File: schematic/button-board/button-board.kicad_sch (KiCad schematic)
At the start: 30 parts, among them J10 Screw_Terminal_01x04, J11 Screw_Terminal_01x04, J3 Screw_Terminal_01x02, J4 Screw_Terminal_01x04, J5 Screw_Terminal_01x04, J6 Screw_Terminal_01x04, J7 Screw_Terminal_01x04, J8 Screw_Terminal_01x04, J9 Screw_Terminal_01x04, U1 MCP23017_SO, U2 ULN2803A

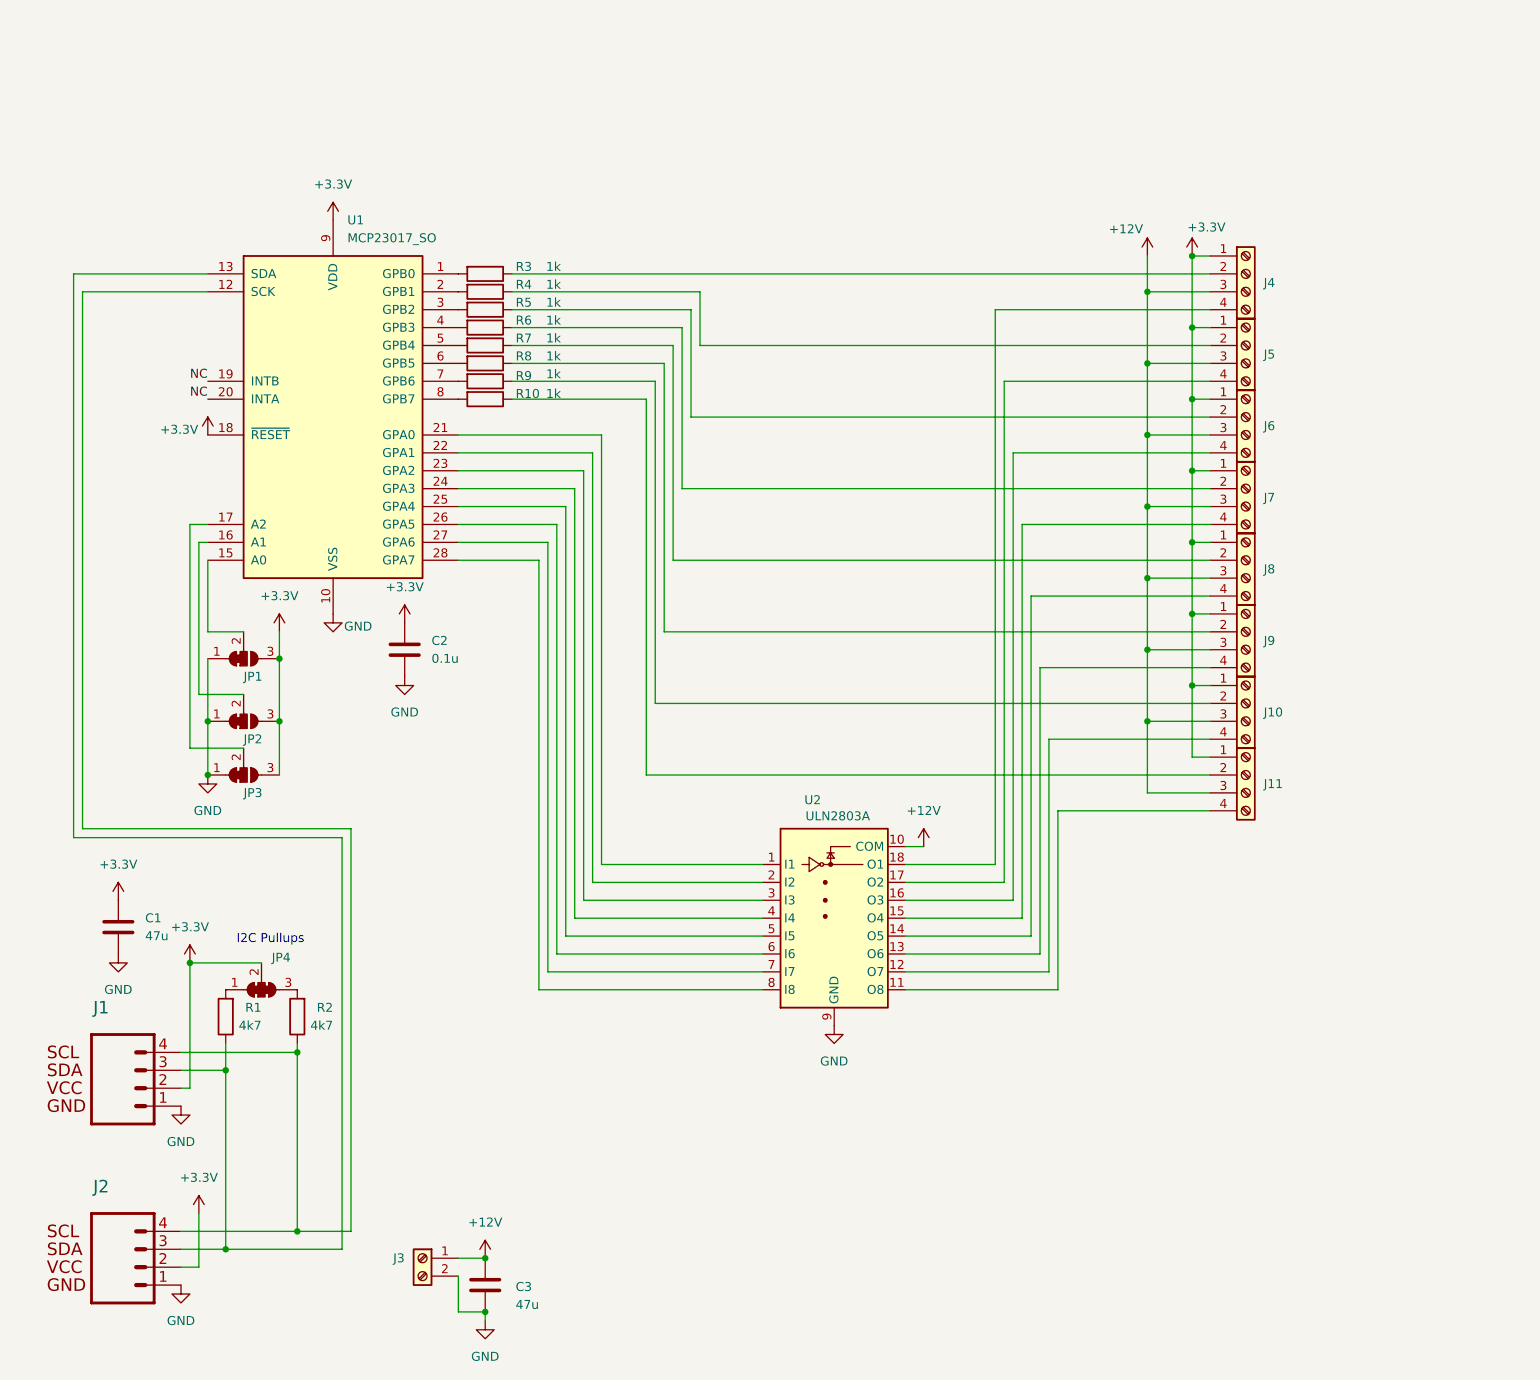
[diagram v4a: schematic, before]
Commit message: updated net labels for pcb layout, added sender board
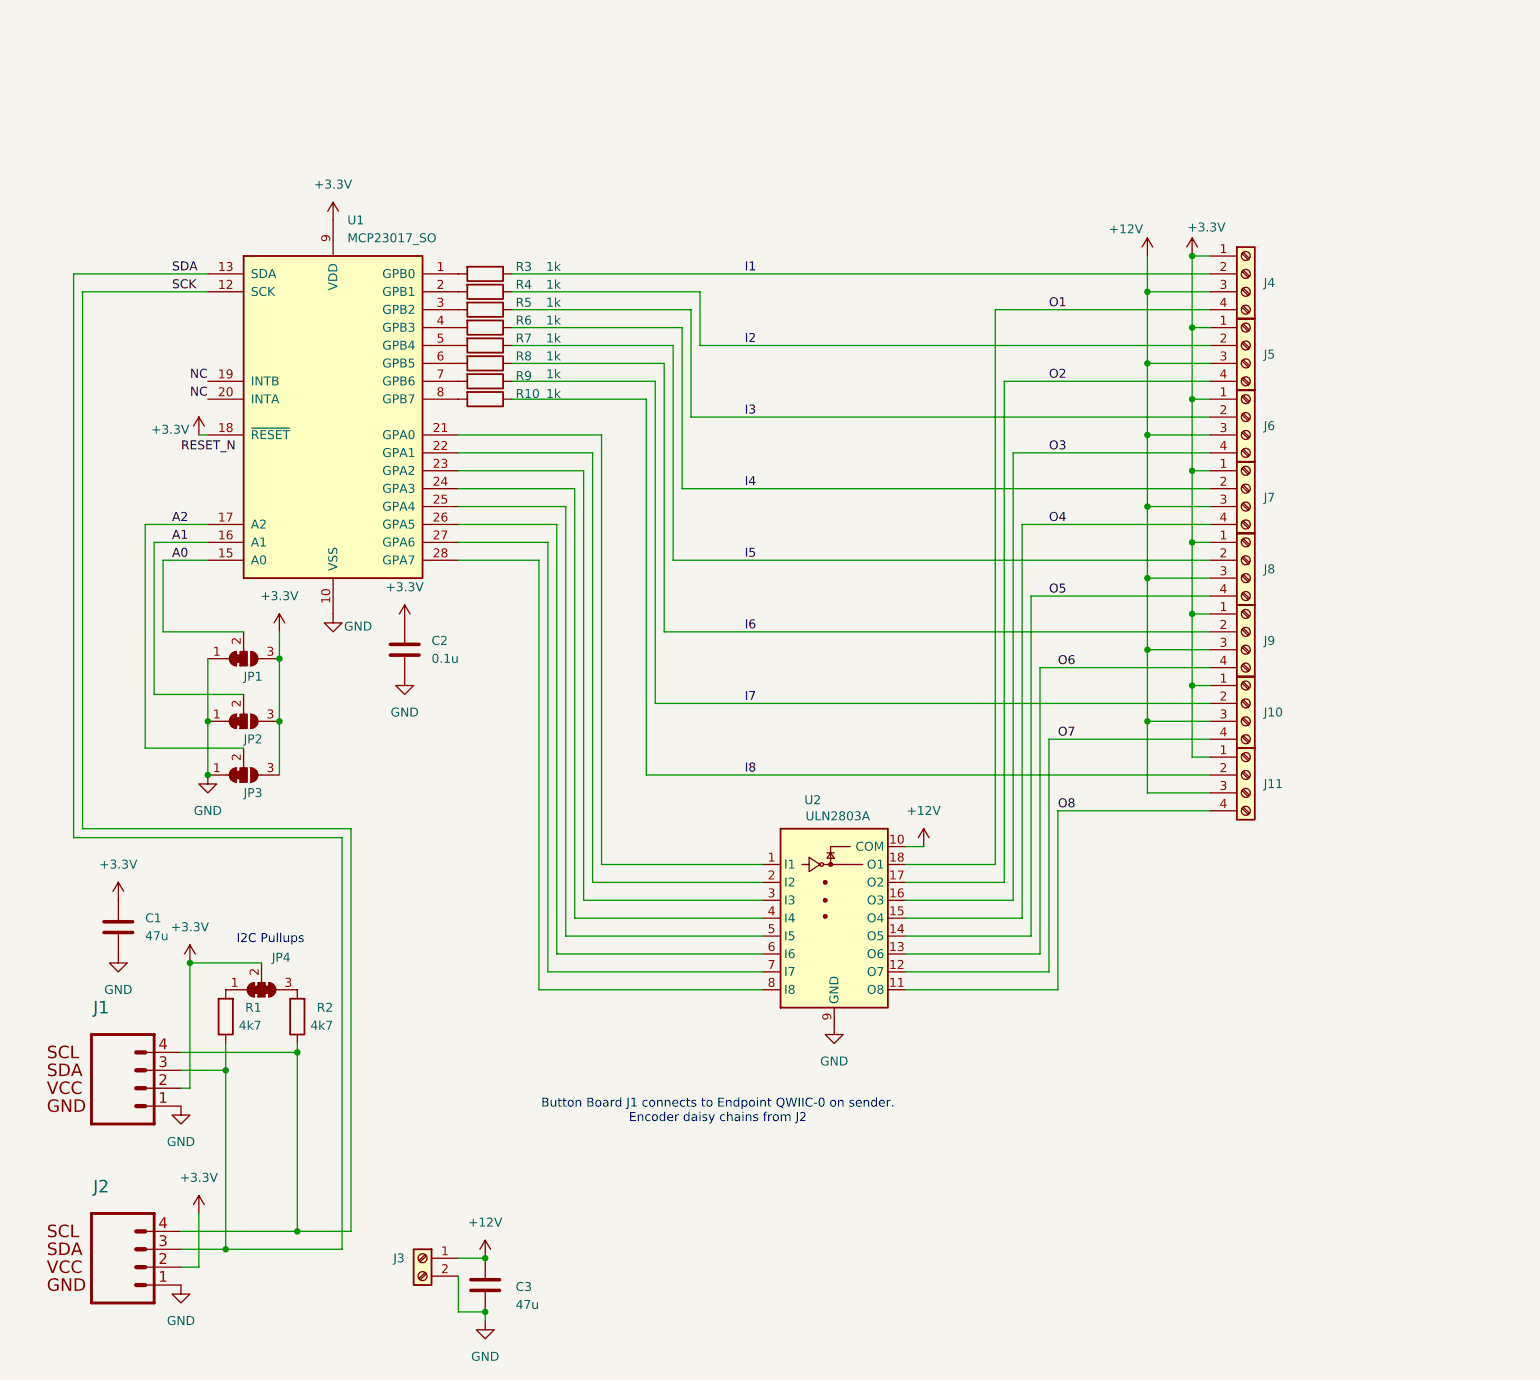
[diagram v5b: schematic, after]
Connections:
- net I4: now reaches J7.2 (Pin_2), R6.1
- net O4: now reaches J7.4 (Pin_4), U2.15 (O4)
- net I5: now reaches J8.2 (Pin_2), R7.1
- net O5: now reaches J8.4 (Pin_4), U2.14 (O5)
- net I1: now reaches J4.2 (Pin_2), R3.1
- net I2: now reaches J5.2 (Pin_2), R4.1
- net O8: now reaches J11.4 (Pin_4), U2.11 (O8)
- net O7: now reaches J10.4 (Pin_4), U2.12 (O7)
- net O6: now reaches J9.4 (Pin_4), U2.13 (O6)
- net O3: now reaches J6.4 (Pin_4), U2.16 (O3)
- net O2: now reaches J5.4 (Pin_4), U2.17 (O2)
- net O1: now reaches J4.4 (Pin_4), U2.18 (O1)
- net I3: now reaches J6.2 (Pin_2), R5.1
- net A2: now reaches JP3.2 (C), U1.17 (A2)
- net I7: now reaches J10.2 (Pin_2), R9.1
- net SCK: now reaches J1.4, J2.4, R2.1, U1.12 (SCK)
- net A1: now reaches JP2.2 (C), U1.16 (A1)
- net SDA: now reaches J1.3, J2.3, R1.1, U1.13 (SDA)
- net A0: now reaches JP1.2 (C), U1.15 (A0)
- net I8: now reaches J11.2 (Pin_2), R10.1
- net I6: now reaches J9.2 (Pin_2), R8.1
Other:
- note added: "Button Board J1 connects to Endpoint QWIIC-0 on sender. Encoder daisy chains from J2"
